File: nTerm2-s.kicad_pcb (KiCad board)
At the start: 4 copper layers, 153.7 x 55.9 mm, 105 parts, among them J1 VGA, J2 Keyboard, J3 Mouse, J4 Speaker, J5 DE9_Plug_MountingHoles, J6 USB_B_Micro, K1 IM41 3V, K2 IM41 3V, K3 IM41 3V, Q1 BC817, Q2 BC817, Q3 BC817, Q4 BC817, Q5 BC817, SW1 IO0, SW2 RESET, SW3 DEFAULTS, U1 ESP32-WROOM-32, U2 LM386, U3 MAX3232E, U4 CP2102N-Axx-xQFN28, U5 NCP1117-3.3_SOT223

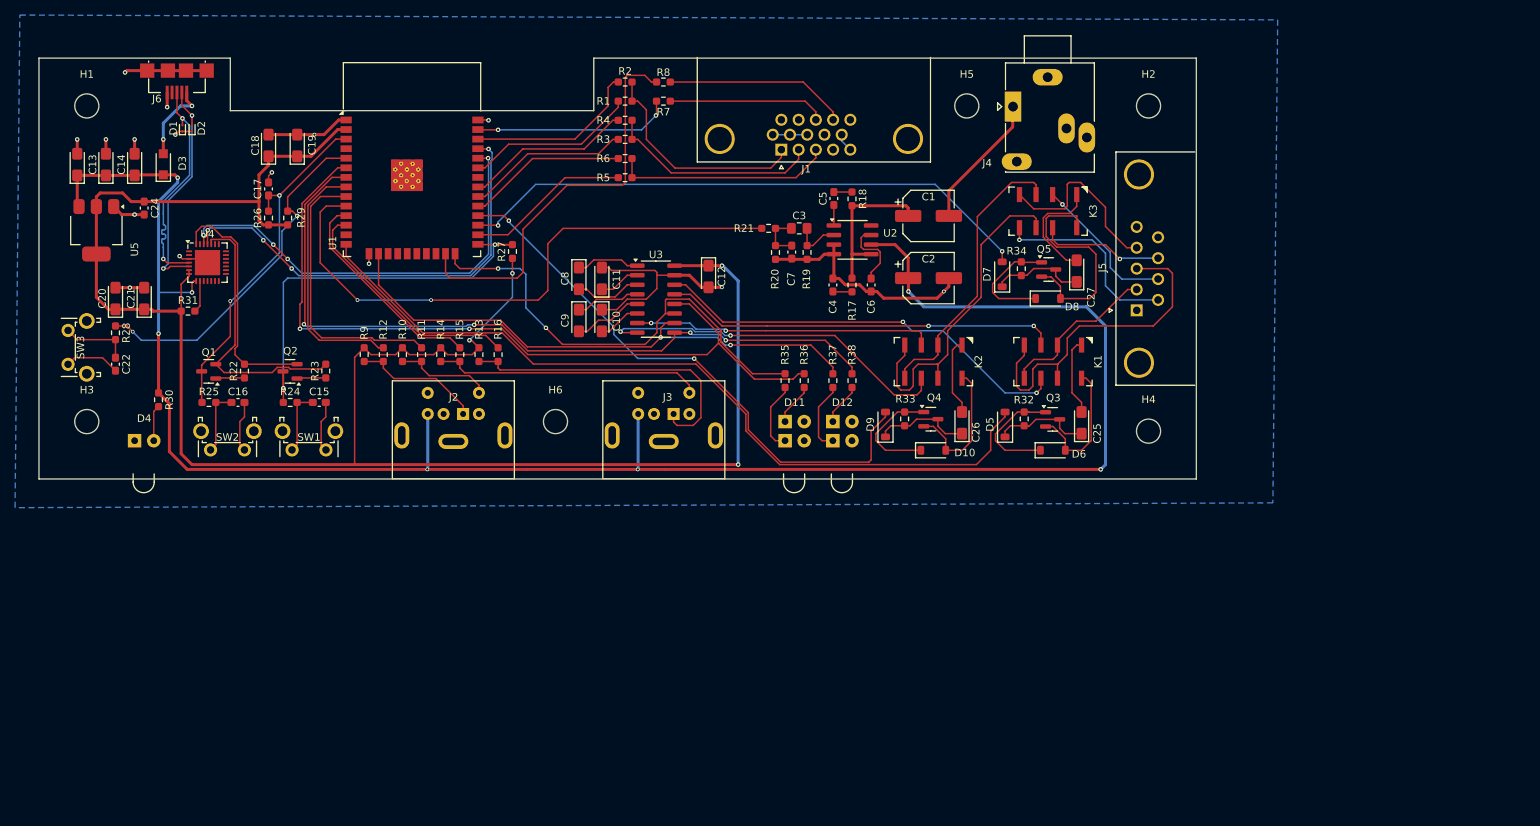
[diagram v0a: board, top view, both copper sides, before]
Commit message: Improvements: - Move 'defaults' button to side, to create space for extra mounting holes. - Change type of USB pug to one with through-hole mounts for extra strength. - Fix audio plug. - Keep some distance around Audio PWM route so we won't get crossover. - Fix missing GND connections on the relay drivers. - Many small improvements to routes. - Relay drivers are tested on breadboard and should work. - Design complete? Maybe an improvement: add SD card slot?
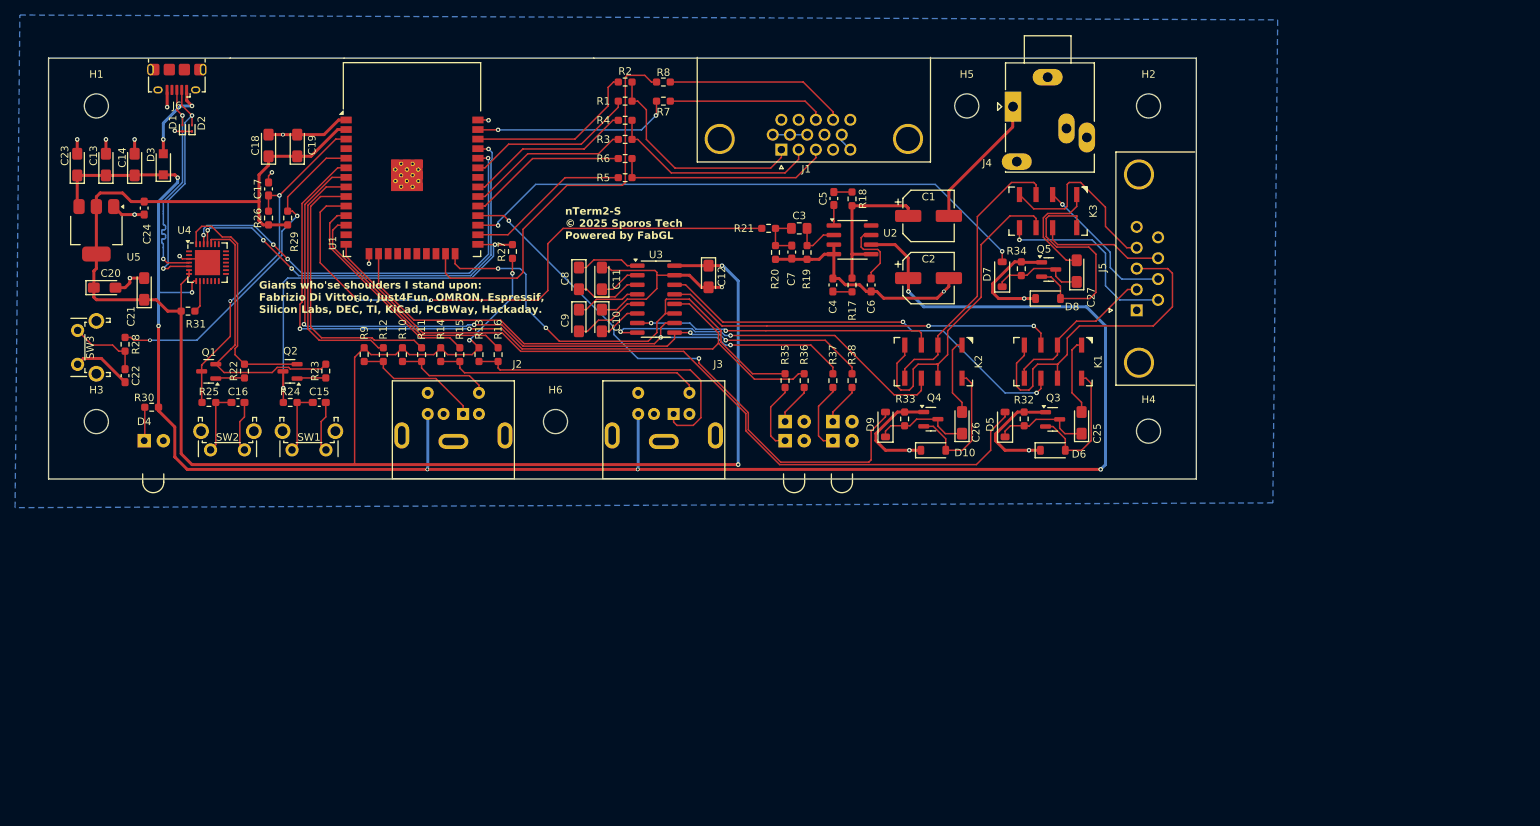
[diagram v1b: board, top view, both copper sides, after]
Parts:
- D11, D12: value LED Dual Low Power 2mA -> LED_Dual_AKAK
- D4: value LED Low Power 2mA -> LED
- J6: footprint SDBox-mini:USB_Micro-B_Unknown_5s_SMT -> Connector_USB:USB_Micro-B_Amphenol_10118194-0001LF_Horizontal
- moved C20 2.03 mm to (35.4, 61.0), turned to 0 degrees
- moved C22 1.98 mm to (38.1, 72.6)
- moved R28 1.98 mm to (38.1, 68.5)
- moved R30 1.35 mm to (41.6, 76.8), turned to 180 degrees
- moved C21 1.27 mm to (40.6, 61.1)
- moved D4 1.27 mm to (40.6, 81.3)
- moved SW3 1.27 mm to (31.8, 71.1)
- moved H1 1.27 mm to (34.3, 36.8)
- moved H3 1.27 mm to (34.3, 78.7)
- moved J6 1.14 mm to (45.0, 33.3)
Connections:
- C1 pad 2: Net-(C1-Pad2) -> Net-(J4-T)
- D10 pad 1: Net-(D10-K) -> GND
- D4 pad 1: GND -> Net-(D4-A)
- D4 pad 2: Net-(D4-A) -> GND
- D6 pad 1: Net-(D6-K) -> GND
- D8 pad 1: Net-(D8-K) -> GND
- Q3 pad 1: Net-(D6-K) -> GND
- Q4 pad 1: Net-(D10-K) -> GND
- Q5 pad 1: Net-(D8-K) -> GND
- R32 pad 2: Net-(D6-K) -> GND
- R33 pad 2: Net-(D10-K) -> GND
- R34 pad 2: Net-(D8-K) -> GND
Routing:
- net GND: track 135.5 -> 171.1 mm, vias 15 -> 17
- net Net-(J4-T): track 0.00 -> 18.0 mm
- net Net-(C1-Pad2): track 18.0 -> 0.00 mm
- net Net-(D6-K): track 15.3 -> 0.00 mm
- net Net-(D10-K): track 15.0 -> 0.00 mm
- net Net-(D8-K): track 14.9 -> 0.00 mm
- net Net-(U1-SENSOR_VN): track 46.9 -> 44.8 mm
- net Net-(C22-Pad1): track 9.20 -> 9.83 mm
- net RXD_2: track 104.6 -> 104.0 mm
- net /_CTS: track 16.7 -> 16.6 mm, vias 1 -> 0
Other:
- board size 153.7 x 55.9 mm -> 152.4 x 55.9 mm
- copper layers 4 -> 2
- board text added: "Giants who'se shoulders I stand upon: Fabrizio Di Vittorio, Just4Fun, OMRON, Espressif, Silicon Labs, DEC, TI, KiCad, PCBWay, Hackaday."
- board text added: "nTerm2-S © 2025 Sporos Tech Powered by FabGL"

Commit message: Made board smaller for easier fitting in enclosure (150x55 or so). Many fixes. All vias are on 1.27 grid. USB-C ocnnector. VGA signal lines all same length, hopefully helping to give good video output.
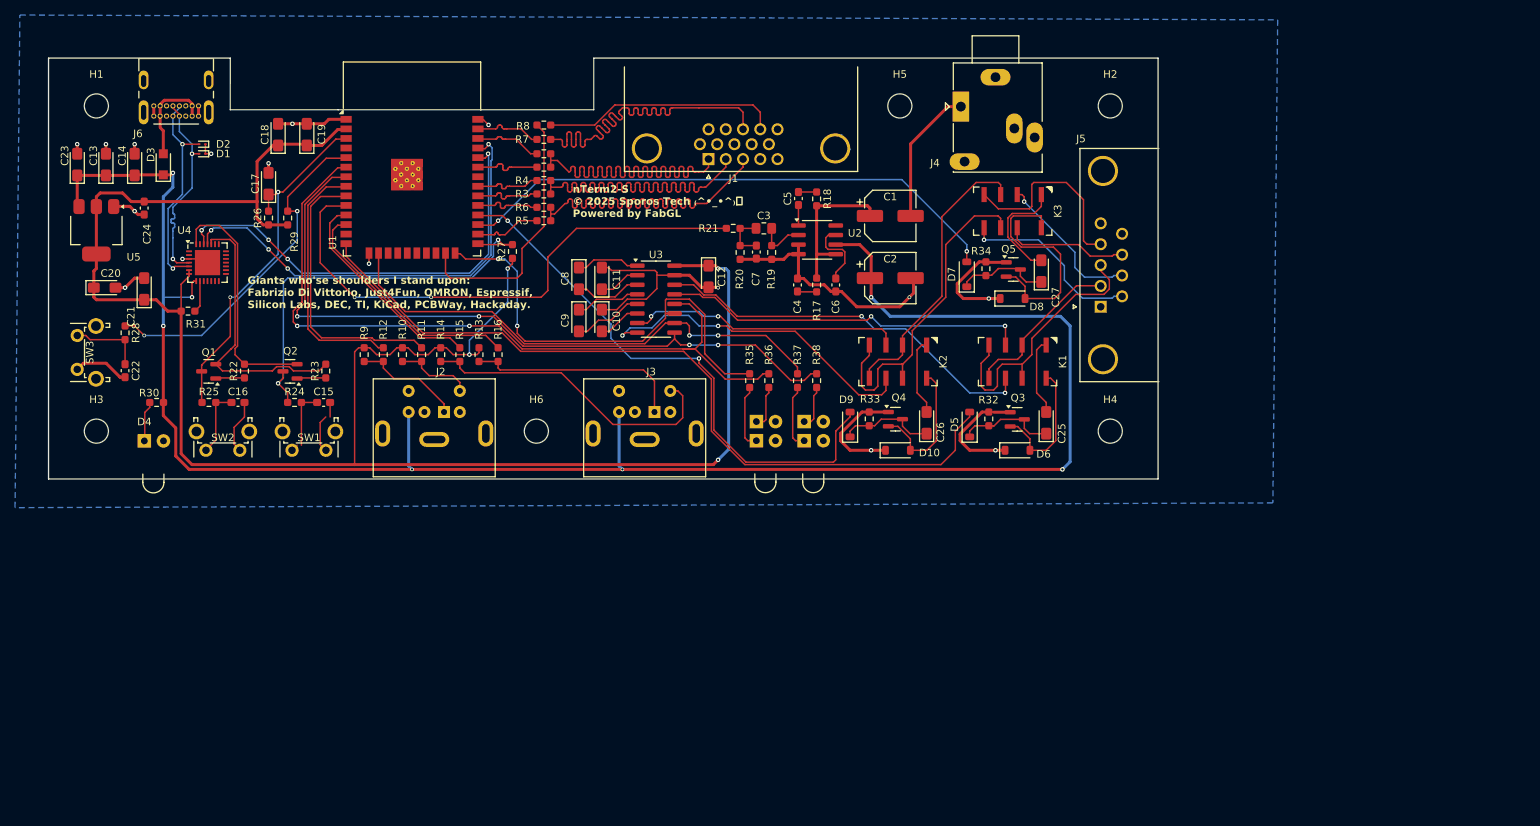
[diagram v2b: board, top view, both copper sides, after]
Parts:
- C17: value 1n -> 1u; footprint Capacitor_SMD:C_0603_1608Metric_Pad1.08x0.95mm_HandSolder -> Capacitor_Tantalum_SMD:CP_EIA-3216-18_Kemet-A_Pad1.58x1.35mm_HandSolder
- C19: value 1u -> 0.1u
- J6: value USB_B_Micro -> USB_C_Receptacle_USB2.0_16P; footprint Connector_USB:USB_Micro-B_Amphenol_10118194-0001LF_Horizontal -> Connector_USB:USB_C_Receptacle_Molex_213716-0001
- moved R8 16.9 mm to (93.7, 39.4)
- moved R7 16.7 mm to (93.7, 41.3)
- moved R2 14.4 mm to (93.7, 43.2)
- moved R1 13.9 mm to (93.7, 45.0)
- moved R4 13.4 mm to (93.7, 46.7)
- moved R3 13.0 mm to (93.7, 48.5)
- moved R6 12.6 mm to (93.7, 50.3)
- moved R5 12.2 mm to (93.7, 52.1)
- moved J1 9.75 mm to (115.6, 43.9)
- moved H5 8.89 mm to (141.0, 36.8)
- moved J4 6.93 mm to (149.1, 36.9)
- moved J6 5.66 mm to (47.9, 38.2)
- moved C1 5.08 mm to (139.7, 51.4)
- moved C2 5.08 mm to (139.7, 59.7)
- moved H2 5.08 mm to (168.9, 36.8)
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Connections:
- C1 pad 2: Net-(J4-T) -> Net-(J4-2)
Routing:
- net Net-(J1-Pad13): track 21.0 -> 55.6 mm
- net Net-(J1-Pad2): track 28.5 -> 57.3 mm
- net Net-(J1-Pad3): track 29.1 -> 57.3 mm
- net Net-(J1-Pad1): track 30.0 -> 57.3 mm
- net VGA_VSYNC: track 53.8 -> 34.4 mm
- net Net-(J4-2): track 0.00 -> 18.3 mm
- net Net-(J4-T): track 18.0 -> 0.00 mm
- net VGA_HSYNC: track 26.2 -> 9.00 mm, vias 2 -> 0
- net VGA_RED_1: track 23.0 -> 9.10 mm
- net VGA_RED_0: track 22.5 -> 8.95 mm
- net VGA_GRN_1: track 22.1 -> 8.96 mm
- net VGA_GRN_0: track 21.5 -> 8.95 mm
- net VGA_BLU_0: track 21.5 -> 8.98 mm
- net Net-(J3-Pad1): track 41.3 -> 29.0 mm
- net VGA_BLU_1: track 21.0 -> 8.95 mm
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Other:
- board size 152.4 x 55.9 mm -> 147.3 x 55.9 mm
- board text added: "nTerm2-S © 2025 Sporos Tech ₍^•_•^₎ﾉ Powered by FabGL"
- board text removed: "nTerm2-S © 2025 Sporos Tech Powered by FabGL"

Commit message: * Final details sorted. Hopefully I've got it all now. * Generated gerbers and sent to JLCPCB for boards to be made. * Fuses for my Fluke 175 multimeter arrived. Experimented with the relay driving circuit. When using 3.3V, 1N4148, BC337, 470u and 3K9, the circuit seems to switch quite reliably. Real circuit is meant to use BAT43 and BC817, but is probably similar enough. Can't switch too fast or the circuit will latch up and stop switching, but 4 times per second seems fine. Circuit uses some 10mA max when switching, and about 1mA continuous when the input is 3.3V.
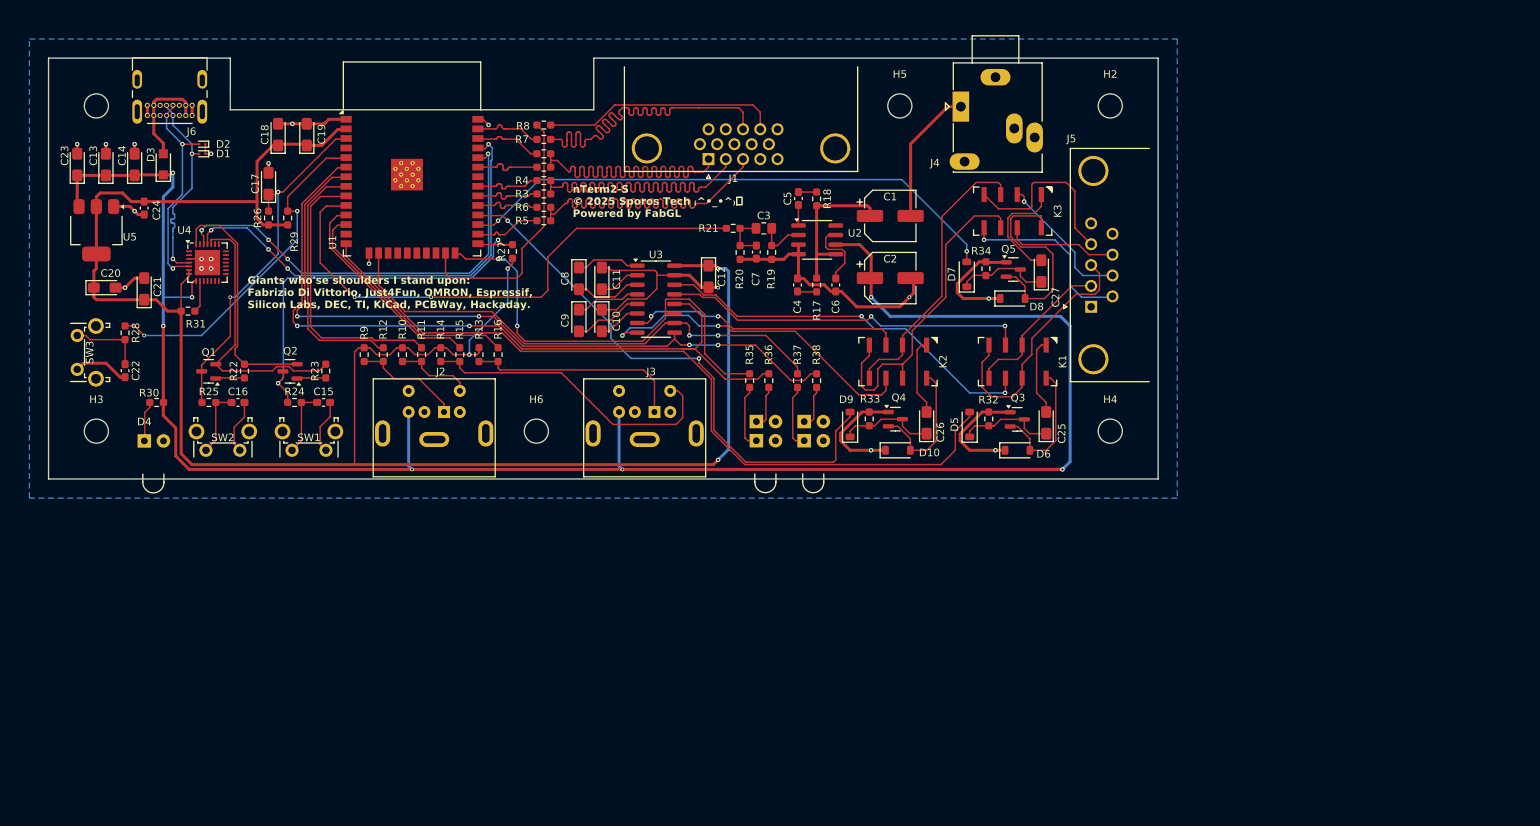
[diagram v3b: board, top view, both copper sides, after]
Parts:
- moved J5 1.27 mm to (166.4, 63.5)
- moved J6 0.85 mm to (47.0, 38.1)
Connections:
- J2 pad 7: (no net) -> GND
- J3 pad 7: (no net) -> GND
- J4 pad R: (no net) -> unconnected-(J4-3-PadR)
- J4 pad RN: (no net) -> unconnected-(J4-5-PadRN)
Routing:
- net RTS_OR_DTR_RLY_-: track 30.6 -> 28.4 mm
- net /_TXD: track 36.5 -> 34.8 mm
- net GND: track 163.6 -> 162.0 mm, vias 16 -> 19
- net /_DTR: track 26.0 -> 24.4 mm
- net /_CTS: track 16.5 -> 15.1 mm
- net /_RTS: track 20.1 -> 18.8 mm
- net /_RXD: track 21.8 -> 20.9 mm
- net Net-(D3-A): track 12.9 -> 13.7 mm

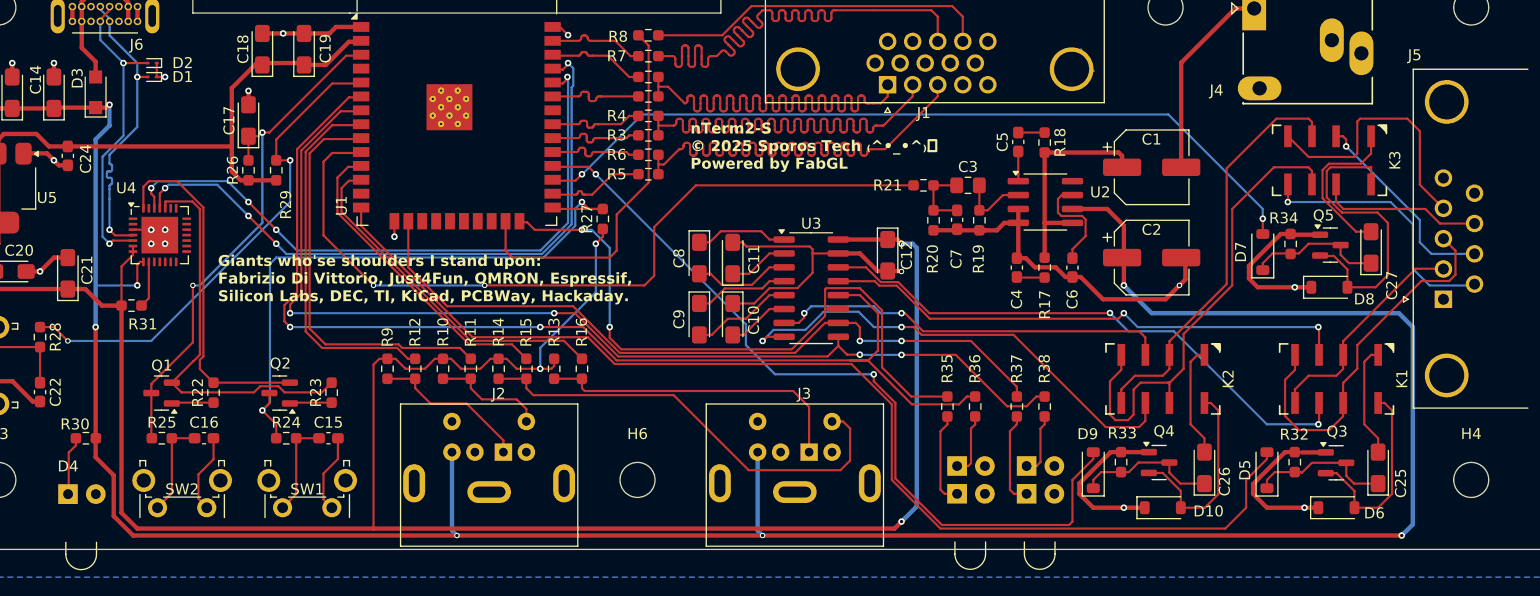
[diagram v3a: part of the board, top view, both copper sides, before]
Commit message: Update wrong footprint for relays K1..K3.
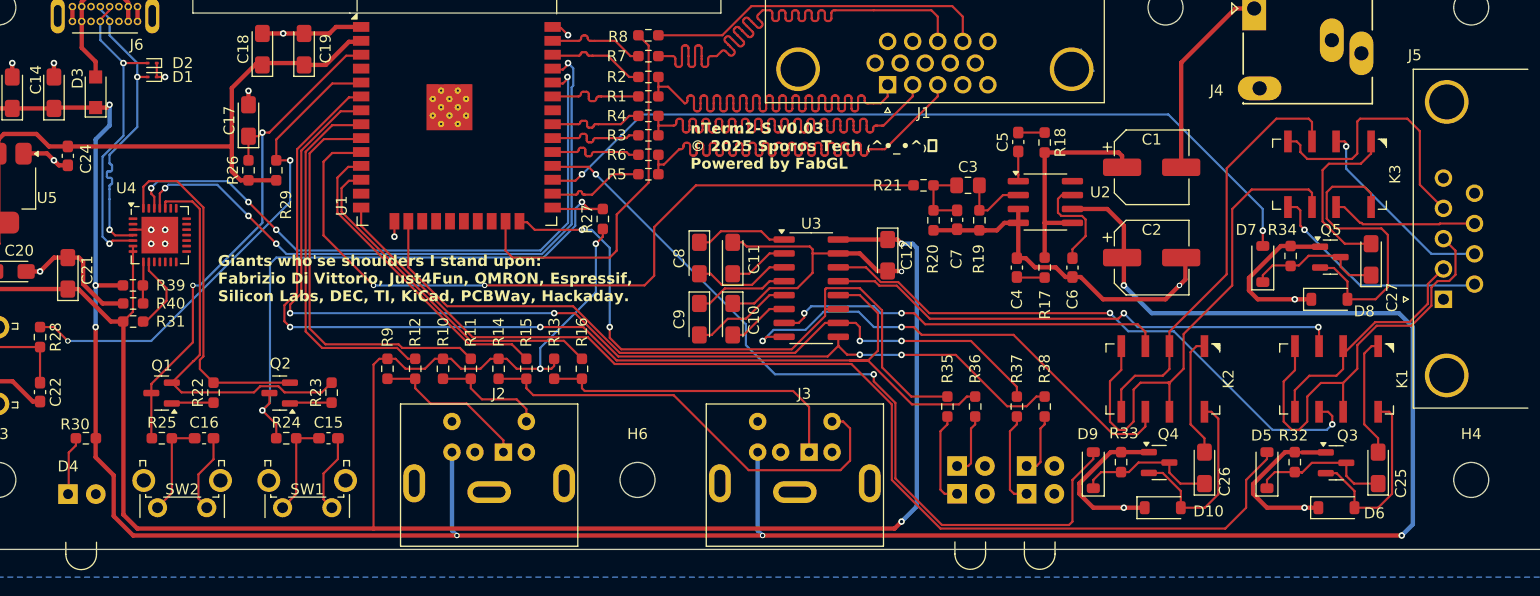
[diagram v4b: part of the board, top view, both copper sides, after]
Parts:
- added R39: 22.1K, Resistor_SMD:R_0603_1608Metric_Pad0.98x0.95mm_HandSolder, F.Cu at (46.6, 62.2)
- added R40: 47.5K, Resistor_SMD:R_0603_1608Metric_Pad0.98x0.95mm_HandSolder, F.Cu at (46.6, 63.9)
- C25, C26, C27: value 220u -> 470u
- K1, K2, K3: footprint Relay_SMD:Relay_DPDT_AXICOM_IMSeries_JLeg -> Relay_SMD:Relay_2P2T_10x6mm_TE_IMxxG
- R32, R33, R34: value 470 -> 3K9
- moved R31 1.46 mm to (46.6, 65.5)
- moved K3 1.27 mm to (156.0, 52.1)
- moved C27 1.10 mm to (159.8, 59.9)
- moved D7 1.10 mm to (149.9, 60.3)
- moved Q5 1.10 mm to (156.0, 59.6)
- moved D8 1.10 mm to (155.9, 63.5)
- moved R34 1.10 mm to (152.4, 59.5)
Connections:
- U4 pad 8: +5V -> Net-(U4-VBUS)
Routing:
- net GND: track 162.0 -> 169.9 mm
- net /_TXD: track 34.8 -> 39.2 mm
- net +5V: track 254.6 -> 250.7 mm
- net Net-(U4-VBUS): track 0.00 -> 3.83 mm
- net /_DSR: track 24.3 -> 20.9 mm
- net Net-(U4-~{RST}): track 4.27 -> 7.43 mm
- net /_CTS_DSR: track 44.7 -> 47.0 mm
- net /TxD: track 51.8 -> 53.7 mm
- net /_CTS: track 15.1 -> 13.4 mm
- net /_RTS_DTR: track 38.0 -> 39.3 mm
- net RTS_OR_DTR_RLY_+: track 14.9 -> 16.1 mm
- net /_RXD: track 20.9 -> 22.0 mm
- net RTS_CTS_OR_DTR_DSR: track 73.3 -> 74.4 mm
- net RTS_CTS_REV_RLY_+: track 10.3 -> 11.2 mm
- net /RxD: track 48.6 -> 47.8 mm
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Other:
- board text added: "nTerm2-S v0.03 © 2025 Sporos Tech ₍^•_•^₎ﾉ Powered by FabGL"
- board text removed: "nTerm2-S © 2025 Sporos Tech ₍^•_•^₎ﾉ Powered by FabGL"
